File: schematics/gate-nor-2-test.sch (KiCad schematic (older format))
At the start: 1 part

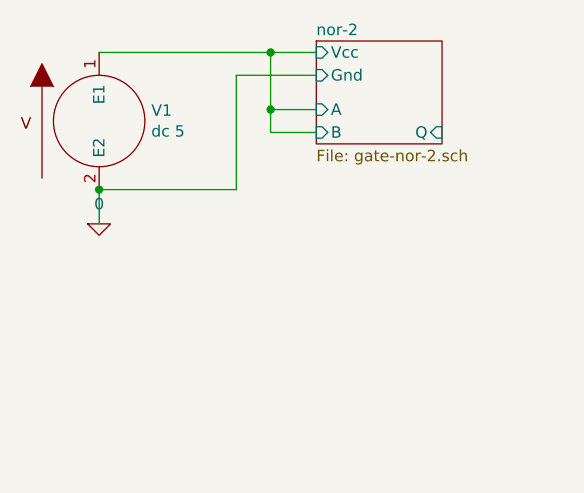
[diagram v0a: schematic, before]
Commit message: Adds some tests for and-2, nor-2, nor-3
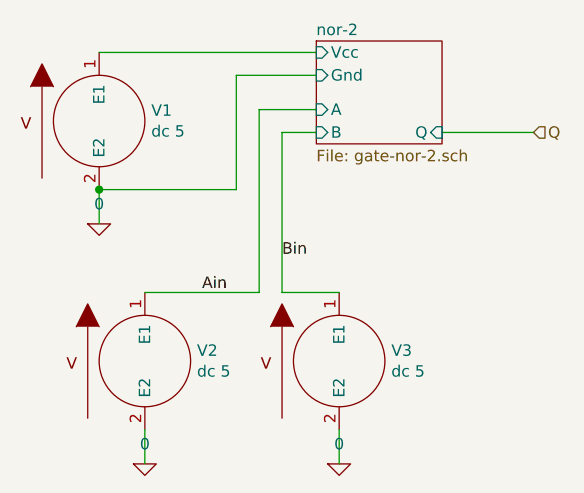
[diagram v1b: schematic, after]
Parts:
- added V2, V3: dc 5, symbol pspice:VSOURCE
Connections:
- net 0: now also V2.2 (E2), V3.2 (E2)
- net nor-2/A renamed nor-2/Vcc
- new net Ain: V2.1 (E1)
- new net Bin: V3.1 (E1)
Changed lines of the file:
@@
 EESchema Schematic File Version 4
+LIBS:gate-nor-2-test-cache
 EELAYER 26 0
 EELAYER END
@@
 $EndDescr
 $Comp
-L pspice:0 #GND0101
+L pspice:0 #GND01
 U 1 1 5C3FDD6E
 P 4450 3850
-F 0 "#GND0101" H 4450 3750 50  0001 C CNN
+F 0 "#GND01" H 4450 3750 50  0001 C CNN
 F 1 "0" H 4450 3937 50  0000 C CNN
 F 2 "" H 4450 3850 50  0001 C CNN
@@
 $EndSheet
 Wire Wire Line
-	4450 3100 5200 3100
-Wire Wire Line
 	5400 3200 5050 3200
 Wire Wire Line
@@
 Connection ~ 4450 3700
 Wire Wire Line
-	5400 3350 5200 3350
+	4450 3100 5400 3100
+Text HLabel 6350 3450 2    50   Input ~ 0
+Q
 Wire Wire Line
-	5200 3350 5200 3100
-Connection ~ 5200 3100
+	6350 3450 5950 3450
+$Comp
+L pspice:0 #GND02
+U 1 1 5C56965D
+P 4650 4900
+F 0 "#GND02" H 4650 4800 50  0001 C CNN
+F 1 "0" H 4650 4987 50  0000 C CNN
+F 2 "" H 4650 4900 50  0001 C CNN
+F 3 "~" H 4650 4900 50  0001 C CNN
+	1    4650 4900
+	1    0    0    -1
+$EndComp
+$Comp
+L pspice:VSOURCE V2
+U 1 1 5C569663
+P 4650 4450
+F 0 "V2" H 4878 4496 50  0000 L CNN
+F 1 "dc 5" H 4878 4405 50  0000 L CNN
+F 2 "" H 4650 4450 50  0001 C CNN
+F 3 "~" H 4650 4450 50  0001 C CNN
+	1    4650 4450
+	1    0    0    -1
+$EndComp
 Wire Wire Line
-	5200 3100 5400 3100
+	4650 4750 4650 4900
+$Comp
+L pspice:0 #GND03
+U 1 1 5C569794
+P 5500 4900
+F 0 "#GND03" H 5500 4800 50  0001 C CNN
+F 1 "0" H 5500 4987 50  0000 C CNN
+F 2 "" H 5500 4900 50  0001 C CNN
+F 3 "~" H 5500 4900 50  0001 C CNN
+	1    5500 4900
+	1    0    0    -1
+$EndComp
+$Comp
+L pspice:VSOURCE V3
+U 1 1 5C56979A
+P 5500 4450
+F 0 "V3" H 5728 4496 50  0000 L CNN
+F 1 "dc 5" H 5728 4405 50  0000 L CNN
+F 2 "" H 5500 4450 50  0001 C CNN
+F 3 "~" H 5500 4450 50  0001 C CNN
+	1    5500 4450
+	1    0    0    -1
+$EndComp
 Wire Wire Line
-	5400 3450 5200 3450
+	5500 4750 5500 4900
 Wire Wire Line
-	5200 3450 5200 3350
-Connection ~ 5200 3350
+	4650 4150 5150 4150
+Wire Wire Line
+	5150 4150 5150 3350
+Wire Wire Line
+	5150 3350 5400 3350
+Wire Wire Line
+	5400 3450 5250 3450
+Wire Wire Line
+	5250 3450 5250 4150
+Wire Wire Line
+	5250 4150 5500 4150
+Text Label 5250 4000 0    50   ~ 0
+Bin
+Text Label 4900 4150 0    50   ~ 0
+Ain
 $EndSCHEMATC
